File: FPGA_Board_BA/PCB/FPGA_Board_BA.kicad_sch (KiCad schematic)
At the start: 0 parts

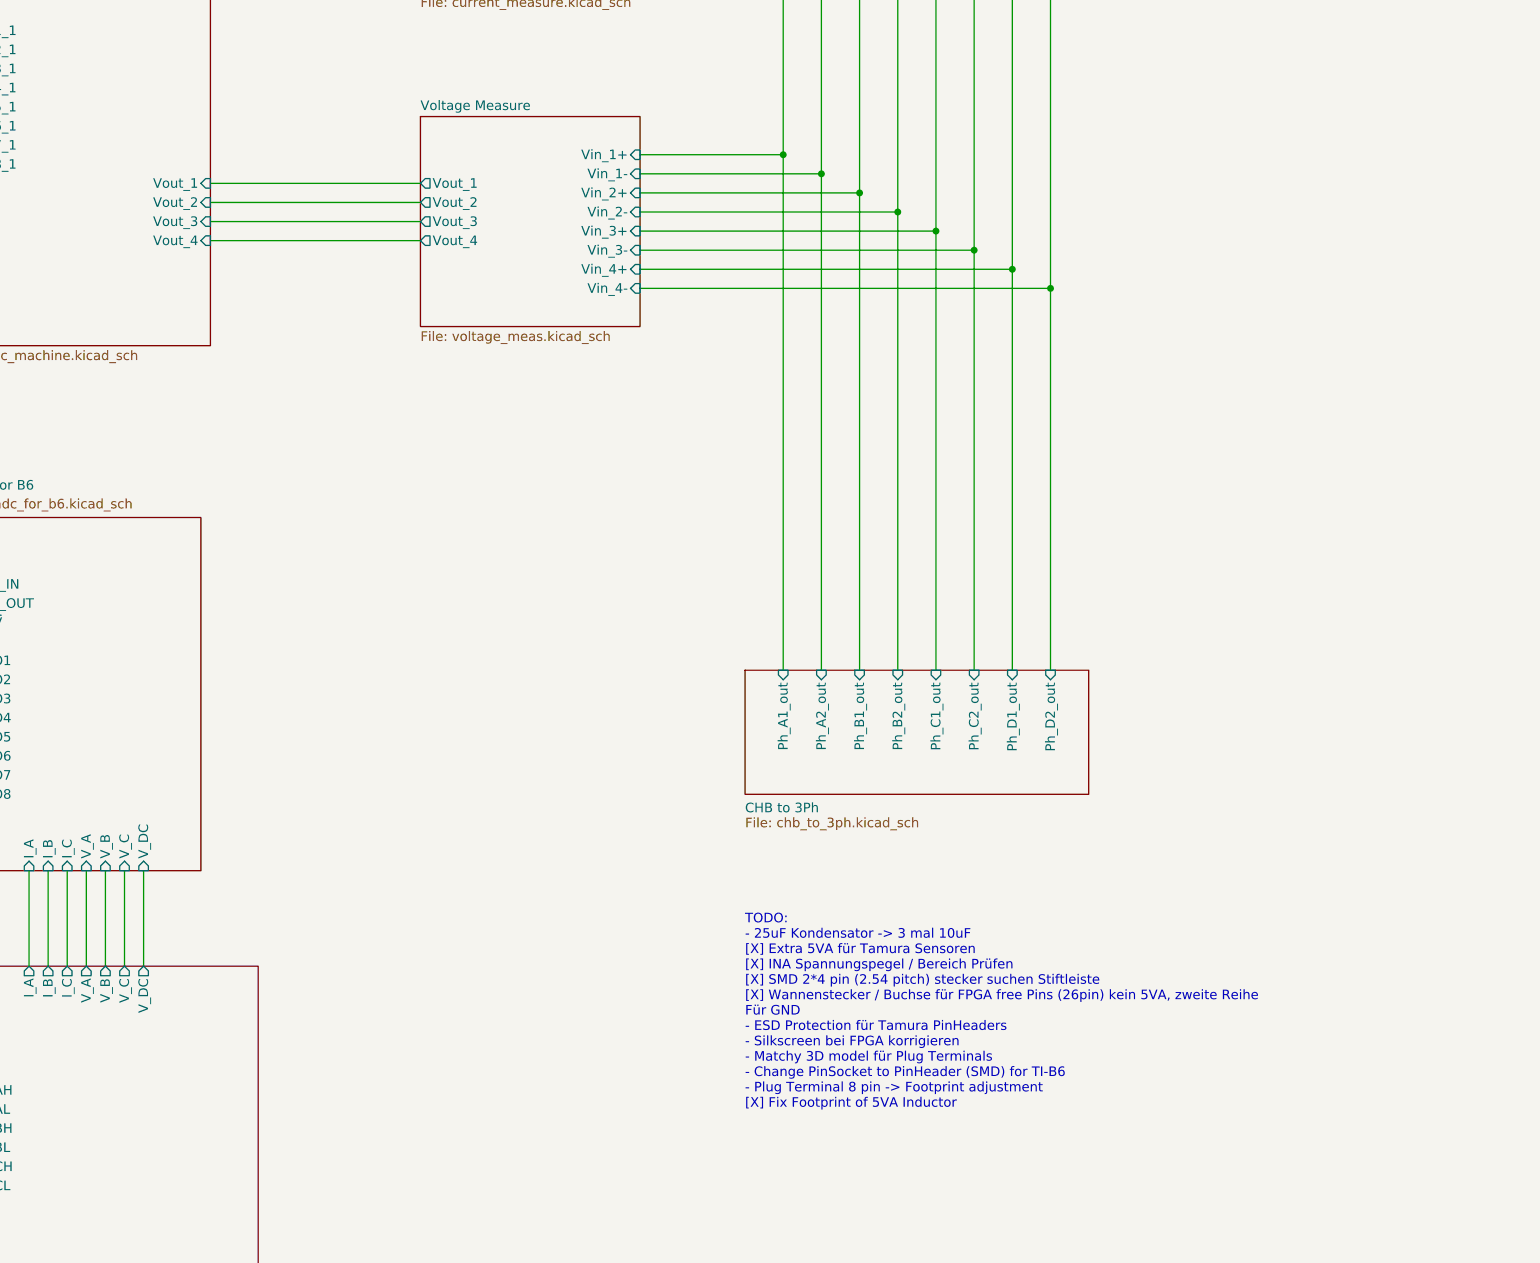
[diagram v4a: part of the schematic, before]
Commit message: component placement with new concept is ready
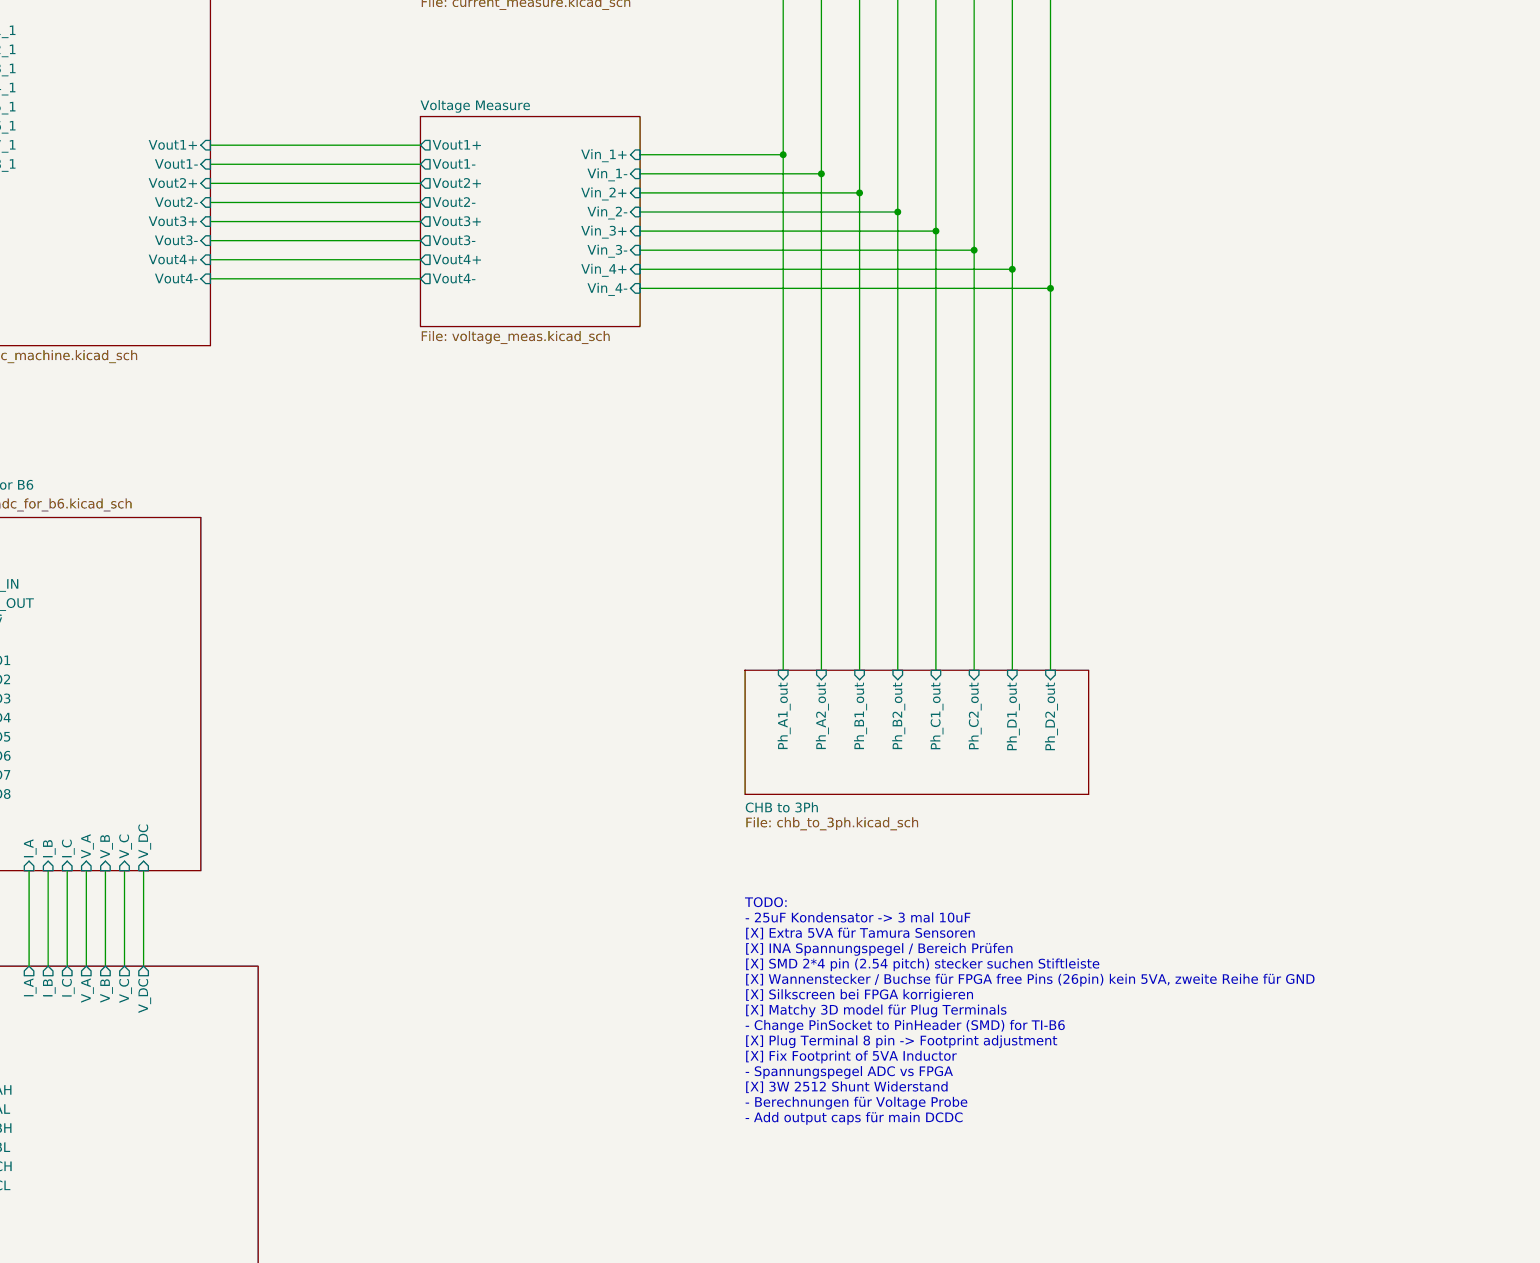
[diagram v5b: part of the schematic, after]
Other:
- sheet ADC for Machine ports: added Vout1+, Vout1-, Vout2+, Vout2-, Vout3+, Vout3-, Vout4+, Vout4-; removed Vout_1, Vout_2, Vout_3, Vout_4
- sheet Voltage Measure ports: added Vout1+, Vout1-, Vout2+, Vout2-, Vout3+, Vout3-, Vout4+, Vout4-; removed Vout_1, Vout_2, Vout_3, Vout_4
- note added: "TODO: - 25uF Kondensator -> 3 mal 10uF [X] Extra 5VA für Tamura Sensoren [X] INA Spannungspegel / Bereich Prüfen [X] SMD 2*4 pin (2.54 pitch) stecker suchen Stiftleiste [X] Wannenstecker / Buchse für FPGA free Pins (26pin) kein 5VA, zweite Reihe für GND [X] Silkscreen bei FPGA korrigieren [X] Matchy 3D model für Plug Terminals - Change PinSocket to PinHeader (SMD) for TI-B6 [X] Plug Terminal 8 pi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"
- note removed: "TODO: - 25uF Kondensator -> 3 mal 10uF [X] Extra 5VA für Tamura Sensoren [X] INA Spannungspegel / Bereich Prüfen [X] SMD 2*4 pin (2.54 pitch) stecker suchen Stiftleiste [X] Wannenstecker / Buchse für FPGA free Pins (26pin) kein 5VA, zweite Reihe Für GND - ESD Protection für Tamura PinHeaders - Silkscreen bei FPGA korrigieren - Matchy 3D model für Plug Terminals - Change PinSocket to PinHeader (SM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"
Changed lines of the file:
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@@
 	(generator_version "9.0")
 	(paper "A3")
-	(text "TODO:\n- 25uF Kondensator -> 3 mal 10uF \n[X] Extra 5VA für Tamura Sensoren\n[X] INA Spannungspegel / Bereich Prüfen\n[X] SMD 2*4 pin (2.54 pitch) stecker suchen Stiftleiste\n[X] Wannenstecker / Buchse für FPGA free Pins (26pin) kein 5VA, zweite Reihe\nFür GND\n- ESD Protection für Tamura PinHeaders\n- Silkscreen bei FPGA korrigieren\n- Matchy 3D model für Plug Terminals\n- Change PinSocket to PinHeader (SMD) for TI-B6\n- Plug Terminal 8 pin -> Footprint adjustment\n[X] Fix Footprint of 5VA Inductor"
+	(text "TODO:\n- 25uF Kondensator -> 3 mal 10uF \n[X] Extra 5VA für Tamura Sensoren\n[X] INA Spannungspegel / Bereich Prüfen\n[X] SMD 2*4 pin (2.54 pitch) stecker suchen Stiftleiste\n[X] Wannenstecker / Buchse für FPGA free Pins (26pin) kein 5VA, zweite Reihe für GND\n[X] Silkscreen bei FPGA korrigieren\n[X] Matchy 3D model für Plug Terminals\n- Change PinSocket to PinHeader (SMD) for TI-B6\n[X] Plug Terminal 8 pin -> Footprint adjustment\n[X] Fix Footprint of 5VA Inductor\n- Spannungspegel ADC vs FPGA\n[X] 3W 2512 Shunt Widerstand\n- Berechnungen für Voltage Probe\n- Add output caps für main DCDC"
 		(exclude_from_sim no)
 		(at 327.66 232.156 0)
@@
 	(wire
 		(pts
+			(xy 256.54 124.46) (xy 284.48 124.46)
+		)
+		(stroke
+			(width 0)
+			(type default)
+		)
+	)
+	(wire
+		(pts
 			(xy 116.84 246.38) (xy 156.21 246.38)
 		)
@@
 	(wire
 		(pts
-			(xy 256.54 127) (xy 284.48 127)
-		)
-		(stroke
-			(width 0)
-			(type default)
-		)
-	)
-	(wire
-		(pts
 			(xy 313.69 128.27) (xy 353.06 128.27)
 		)
@@
 	(wire
 		(pts
-			(xy 256.54 129.54) (xy 284.48 129.54)
-		)
-		(stroke
-			(width 0)
-			(type default)
-		)
-	)
-	(wire
-		(pts
 			(xy 242.57 213.36) (xy 242.57 226.06)
 		)
@@
 	(wire
 		(pts
+			(xy 256.54 121.92) (xy 284.48 121.92)
+		)
+		(stroke
+			(width 0)
+			(type default)
+		)
+	)
+	(wire
+		(pts
 			(xy 337.82 120.65) (xy 337.82 186.69)
 		)
@@
 	(wire
 		(pts
+			(xy 256.54 127) (xy 284.48 127)
+		)
+		(stroke
+			(width 0)
+			(type default)
+		)
+	)
+	(wire
+		(pts
 			(xy 353.06 85.09) (xy 353.06 128.27)
 		)
@@
 	(wire
 		(pts
+			(xy 256.54 129.54) (xy 284.48 129.54)
+		)
+		(stroke
+			(width 0)
+			(type default)
+		)
+	)
+	(wire
+		(pts
 			(xy 313.69 118.11) (xy 332.74 118.11)
 		)
@@
 	(wire
 		(pts
-			(xy 256.54 124.46) (xy 284.48 124.46)
-		)
-		(stroke
-			(width 0)
-			(type default)
-		)
-	)
-	(wire
-		(pts
 			(xy 198.12 252.73) (xy 220.98 252.73)
 		)
@@
 	(wire
 		(pts
+			(xy 256.54 132.08) (xy 284.48 132.08)
+		)
+		(stroke
+			(width 0)
+			(type default)
+		)
+	)
+	(wire
+		(pts
 			(xy 116.84 186.69) (xy 156.21 186.69)
 		)
@@
 	(wire
 		(pts
+			(xy 256.54 119.38) (xy 284.48 119.38)
+		)
+		(stroke
+			(width 0)
+			(type default)
+		)
+	)
+	(wire
+		(pts
 			(xy 116.84 217.17) (xy 156.21 217.17)
 		)
@@
 	(wire
 		(pts
+			(xy 256.54 134.62) (xy 284.48 134.62)
+		)
+		(stroke
+			(width 0)
+			(type default)
+		)
+	)
+	(wire
+		(pts
 			(xy 116.84 166.37) (xy 156.21 166.37)
 		)
@@
 	(wire
 		(pts
-			(xy 116.84 123.19) (xy 156.21 123.19)
+			(xy 256.54 116.84) (xy 284.48 116.84)
 		)
 		(stroke
@@
 	(wire
 		(pts
-			(xy 342.9 123.19) (xy 342.9 186.69)
+			(xy 116.84 123.19) (xy 156.21 123.19)
 		)
 		(stroke
@@
 	(wire
 		(pts
-			(xy 116.84 151.13) (xy 156.21 151.13)
+			(xy 342.9 123.19) (xy 342.9 186.69)
 		)
 		(stroke
@@
 	(wire
 		(pts
-			(xy 116.84 130.81) (xy 156.21 130.81)
+			(xy 116.84 151.13) (xy 156.21 151.13)
 		)
 		(stroke
@@
 	(wire
 		(pts
-			(xy 116.84 266.7) (xy 156.21 266.7)
+			(xy 116.84 130.81) (xy 156.21 130.81)
 		)
 		(stroke
@@
 	(wire
 		(pts
-			(xy 116.84 133.35) (xy 156.21 133.35)
+			(xy 116.84 266.7) (xy 156.21 266.7)
 		)
 		(stroke
@@
 	(wire
 		(pts
-			(xy 116.84 248.92) (xy 156.21 248.92)
+			(xy 116.84 133.35) (xy 156.21 133.35)
 		)
 		(stroke
@@
 	(wire
 		(pts
-			(xy 256.54 121.92) (xy 284.48 121.92)
+			(xy 116.84 248.92) (xy 156.21 248.92)
 		)
 		(stroke
@@
 			)
 		)
-		(pin "Vout_1" input
-			(at 256.54 121.92 0)
+		(pin "CLK_OUT_1" output
+			(at 222.25 92.71 180)
+			(effects
+				(font
+					(size 1.27 1.27)
+				)
+				(justify left)
+			)
+		)
+		(pin "~{CNV}_1" input
+			(at 222.25 95.25 180)
+			(effects
+				(font
+					(size 1.27 1.27)
+				)
+				(justify left)
+			)
+		)
+		(pin "Iin_1" input
+			(at 256.54 78.74 0)
 			(effects
 				(font
@@
 			)
 		)
-		(pin "Vout_2" input
-			(at 256.54 124.46 0)
+		(pin "Iin_2" input
+			(at 256.54 81.28 0)
 			(effects
 				(font
@@
 			)
 		)
-		(pin "Vout_3" input
-			(at 256.54 127 0)
+		(pin "Iin_3" input
+			(at 256.54 83.82 0)
 			(effects
 				(font
@@
 			)
 		)
-		(pin "Vout_4" input
-			(at 256.54 129.54 0)
+		(pin "Iin_4" input
+			(at 256.54 86.36 0)
 			(effects
 				(font
@@
 			)
 		)
-		(pin "CLK_OUT_1" output
-			(at 222.25 92.71 180)
+		(pin "Vout1+" input
+			(at 256.54 116.84 0)
 			(effects
 				(font
 					(size 1.27 1.27)
 				)
-				(justify left)
+				(justify right)
 			)
 		)
-		(pin "~{CNV}_1" input
-			(at 222.25 95.25 180)
+		(pin "Vout1-" input
+			(at 256.54 119.38 0)
 			(effects
 				(font
 					(size 1.27 1.27)
 				)
-				(justify left)
+				(justify right)
 			)
 		)
-		(pin "Iin_1" input
-			(at 256.54 78.74 0)
+		(pin "Vout2+" input
+			(at 256.54 121.92 0)
 			(effects
 				(font
@@
 			)
 		)
-		(pin "Iin_2" input
-			(at 256.54 81.28 0)
+		(pin "Vout2-" input
+			(at 256.54 124.46 0)
 			(effects
 				(font
@@
 			)
 		)
-		(pin "Iin_3" input
-			(at 256.54 83.82 0)
+		(pin "Vout3+" input
+			(at 256.54 127 0)
 			(effects
 				(font
@@
 			)
 		)
-		(pin "Iin_4" input
-			(at 256.54 86.36 0)
+		(pin "Vout3-" input
+			(at 256.54 129.54 0)
+			(effects
+				(font
+					(size 1.27 1.27)
+				)
+				(justify right)
+			)
+		)
+		(pin "Vout4+" input
+			(at 256.54 132.08 0)
+			(effects
+				(font
+					(size 1.27 1.27)
+				)
+				(justify right)
+			)
+		)
+		(pin "Vout4-" input
+			(at 256.54 134.62 0)
 			(effects
 				(font
@@
 			)
 		)
-		(pin "Vout_1" output
+		(pin "Vout1+" output
+			(at 284.48 116.84 180)
+			(effects
+				(font
+					(size 1.27 1.27)
+				)
+				(justify left)
+			)
+		)
+		(pin "Vout1-" output
+			(at 284.48 119.38 180)
+			(effects
+				(font
+					(size 1.27 1.27)
+				)
+				(justify left)
+			)
+		)
+		(pin "Vout2+" output
 			(at 284.48 121.92 180)
 			(effects
@@
 			)
 		)
-		(pin "Vout_2" output
+		(pin "Vout2-" output
 			(at 284.48 124.46 180)
 			(effects
@@
 			)
 		)
-		(pin "Vout_3" output
+		(pin "Vout3+" output
 			(at 284.48 127 180)
 			(effects
@@
 			)
 		)
-		(pin "Vout_4" output
+		(pin "Vout3-" output
 			(at 284.48 129.54 180)
 			(effects
 				(font
+					(size 1.27 1.27)
+				)
+				(justify left)
+			)
+		)
+		(pin "Vout4+" output
+			(at 284.48 132.08 180)
+			(effects
+				(font
+					(size 1.27 1.27)
+				)
+				(justify left)
+			)
+		)
+		(pin "Vout4-" output
+			(at 284.48 134.62 180)
+			(effects
+				(font

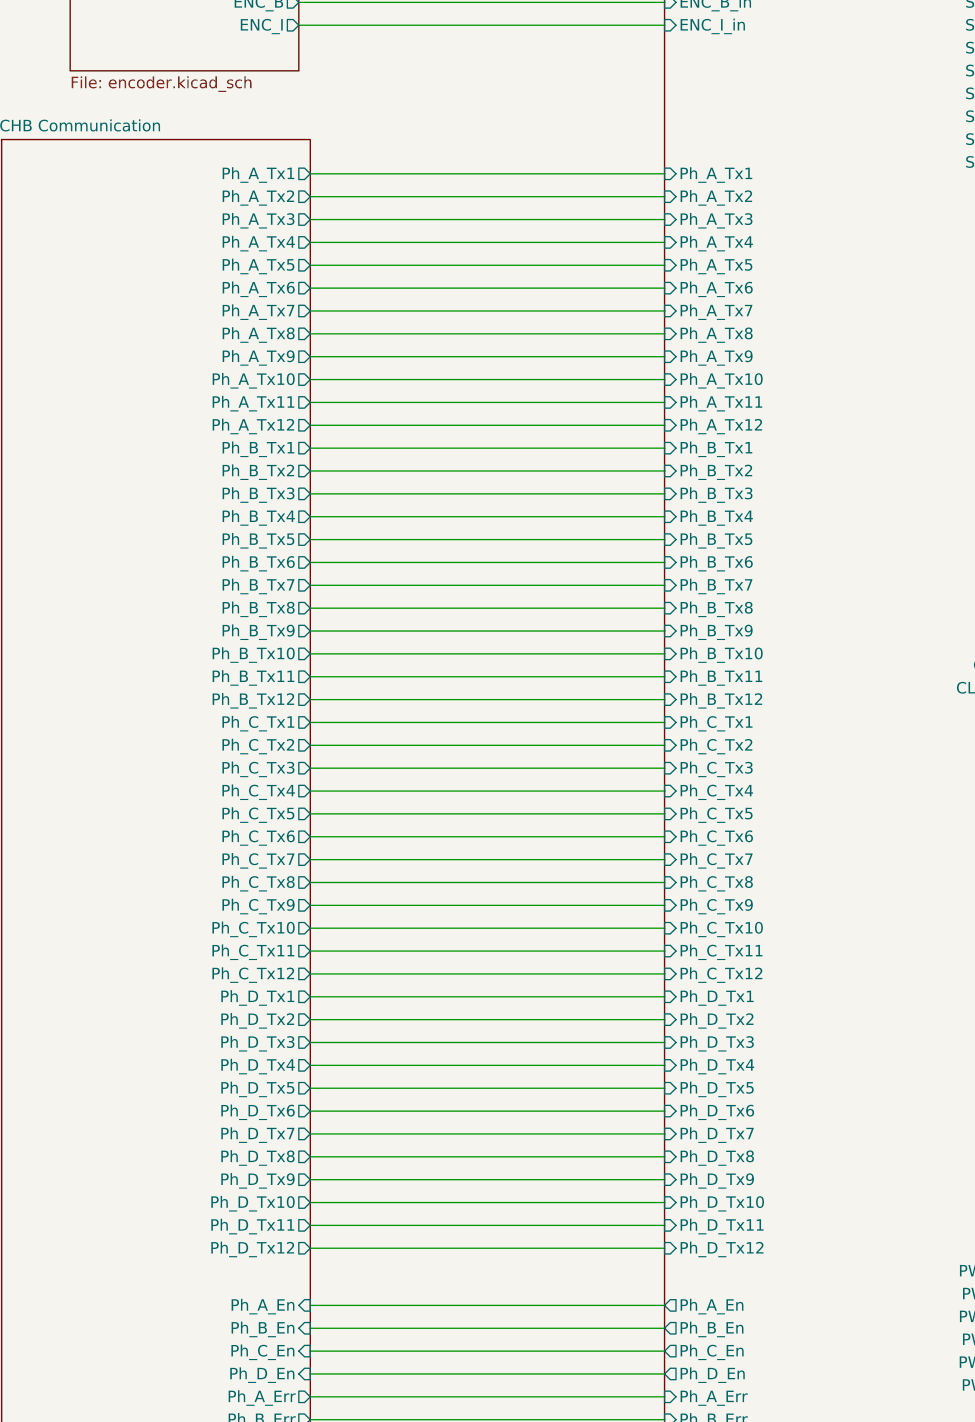
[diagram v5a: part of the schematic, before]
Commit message: added bus into schematic
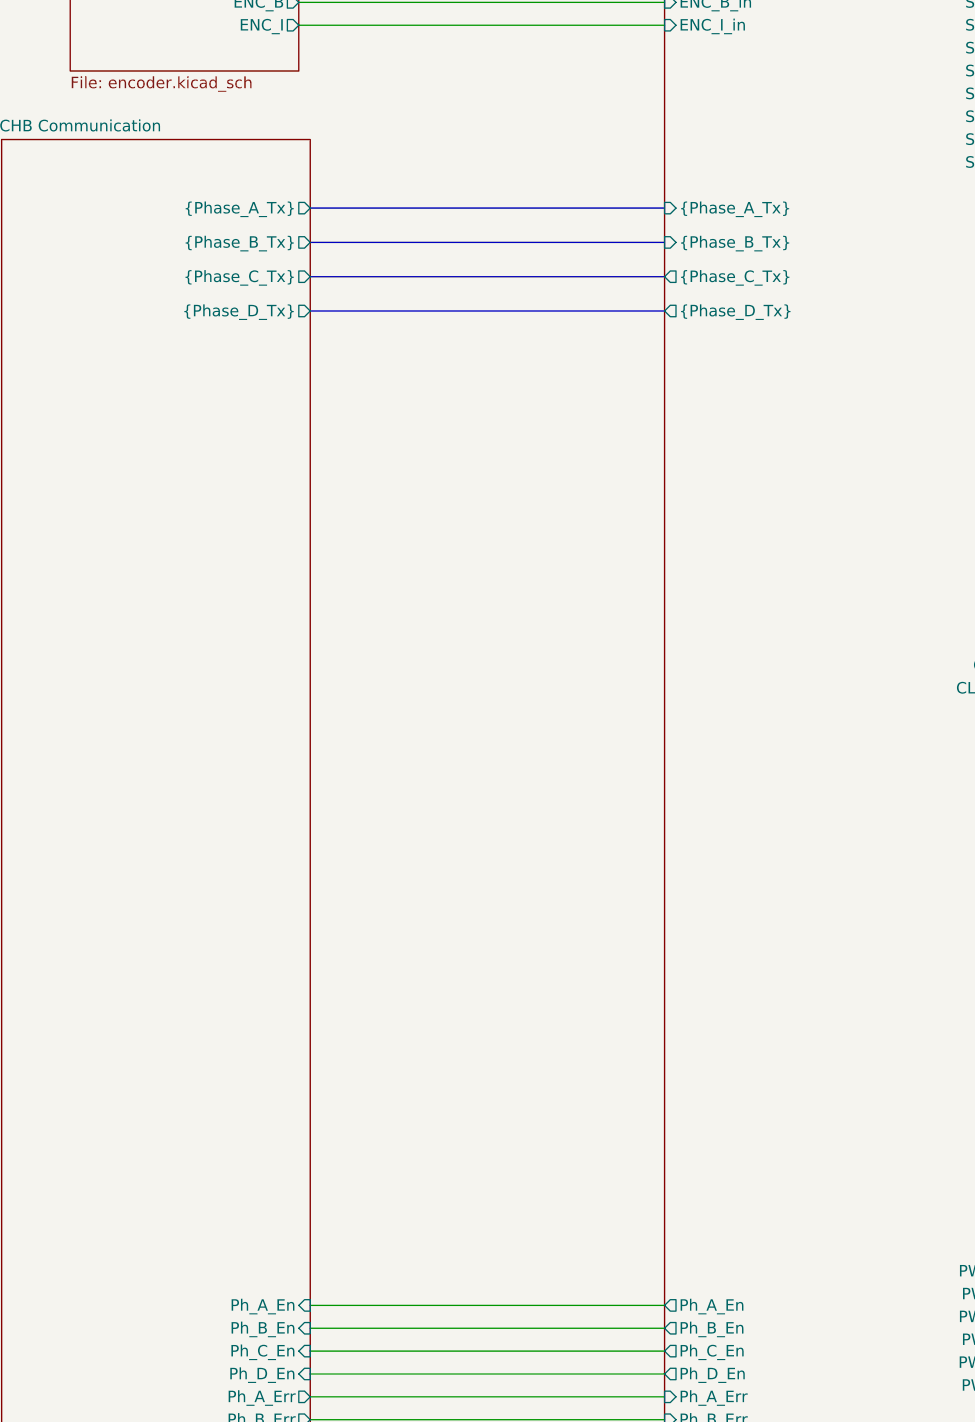
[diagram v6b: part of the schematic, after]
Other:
- sheet CHB Communication ports: added {Phase_A_Tx}, {Phase_B_Tx}, {Phase_C_Tx}, {Phase_D_Tx}; removed Ph_A_Tx1, Ph_A_Tx10, Ph_A_Tx11, Ph_A_Tx12, Ph_A_Tx2, Ph_A_Tx3, Ph_A_Tx4, Ph_A_Tx5, Ph_A_Tx6, Ph_A_Tx7, Ph_A_Tx8, Ph_A_Tx9, Ph_B_Tx1, Ph_B_Tx10, Ph_B_Tx11, Ph_B_Tx12, Ph_B_Tx2, Ph_B_Tx3, Ph_B_Tx4, Ph_B_Tx5, Ph_B_Tx6, Ph_B_Tx7, Ph_B_Tx8, Ph_B_Tx9, Ph_C_Tx1, Ph_C_Tx10, Ph_C_Tx11, Ph_C_Tx12, Ph_C_Tx2, Ph_C_Tx3, Ph_C_Tx4, Ph_C_Tx5, Ph_C_Tx6, Ph_C_Tx7, Ph_C_Tx8, Ph_C_Tx9, Ph_D_Tx1, Ph_D_Tx10, Ph_D_Tx11, Ph_D_Tx12, Ph_D_Tx2, Ph_D_Tx3, Ph_D_Tx4, Ph_D_Tx5, Ph_D_Tx6, Ph_D_Tx7, Ph_D_Tx8, Ph_D_Tx9
- sheet FPGA ports: added {Phase_A_Tx}, {Phase_B_Tx}, {Phase_C_Tx}, {Phase_D_Tx}; removed Ph_A_Tx1, Ph_A_Tx10, Ph_A_Tx11, Ph_A_Tx12, Ph_A_Tx2, Ph_A_Tx3, Ph_A_Tx4, Ph_A_Tx5, Ph_A_Tx6, Ph_A_Tx7, Ph_A_Tx8, Ph_A_Tx9, Ph_B_Tx1, Ph_B_Tx10, Ph_B_Tx11, Ph_B_Tx12, Ph_B_Tx2, Ph_B_Tx3, Ph_B_Tx4, Ph_B_Tx5, Ph_B_Tx6, Ph_B_Tx7, Ph_B_Tx8, Ph_B_Tx9, Ph_C_Tx1, Ph_C_Tx10, Ph_C_Tx11, Ph_C_Tx12, Ph_C_Tx2, Ph_C_Tx3, Ph_C_Tx4, Ph_C_Tx5, Ph_C_Tx6, Ph_C_Tx7, Ph_C_Tx8, Ph_C_Tx9, Ph_D_Tx1, Ph_D_Tx10, Ph_D_Tx11, Ph_D_Tx12, Ph_D_Tx2, Ph_D_Tx3, Ph_D_Tx4, Ph_D_Tx5, Ph_D_Tx6, Ph_D_Tx7, Ph_D_Tx8, Ph_D_Tx9
